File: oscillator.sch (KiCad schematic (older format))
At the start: 32 parts, among them Q1 PMOS, Q10 PMOS, Q11 MOS_Resistor, Q12 PMOS, Q13 PMOS, Q14 PMOS, Q15 MOS_Resistor, Q16 PMOS, Q17 PMOS, Q18 MOS_Resistor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

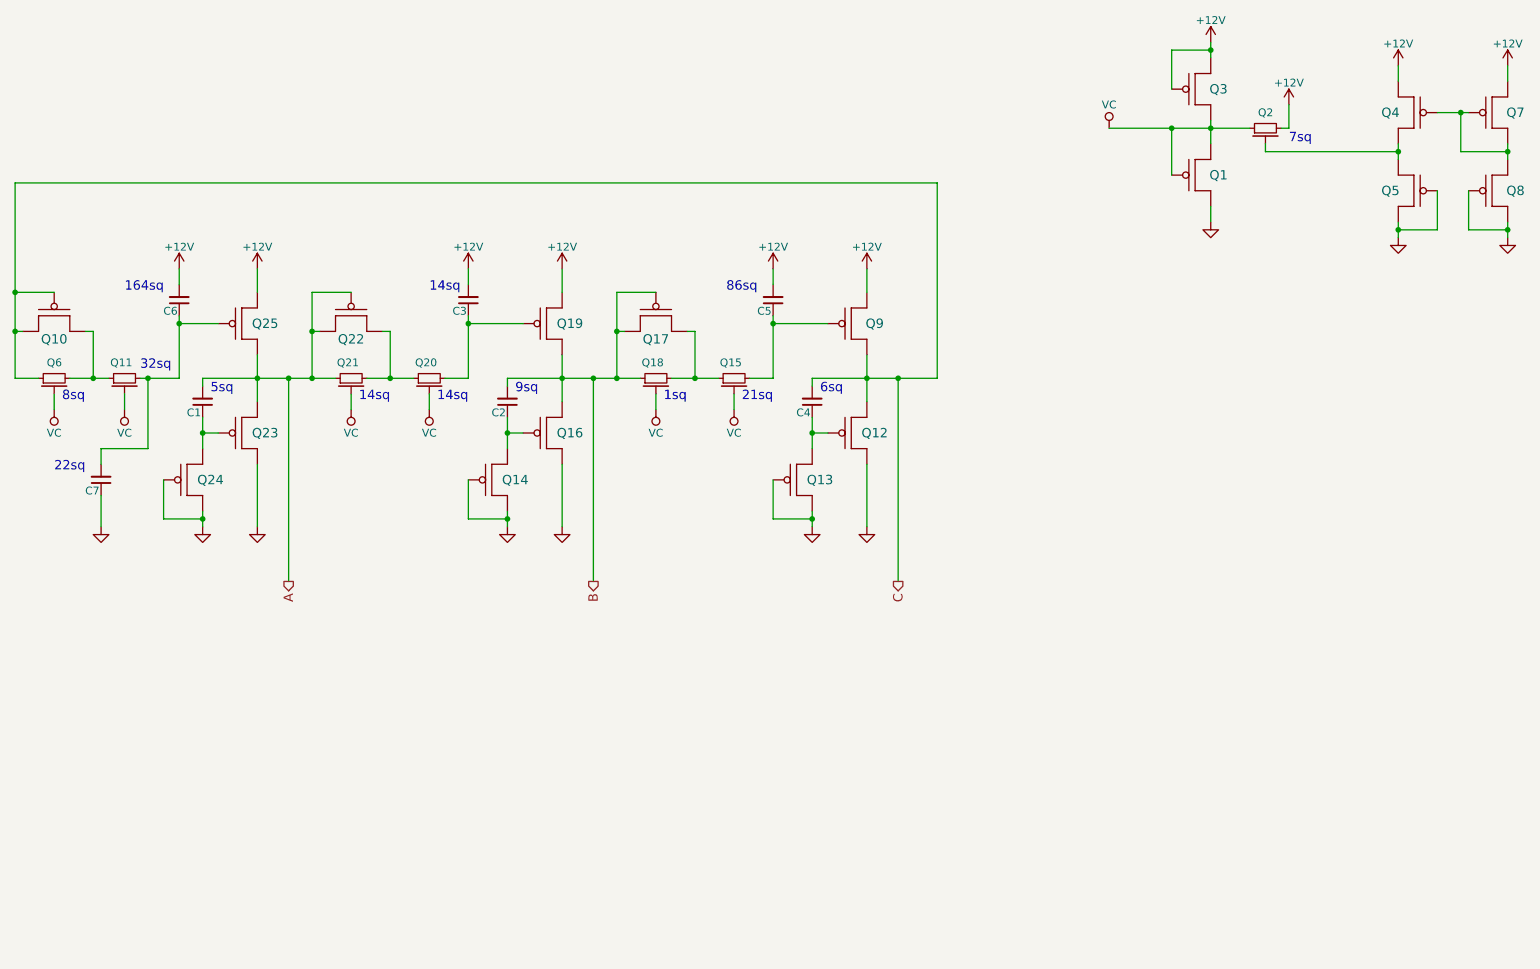
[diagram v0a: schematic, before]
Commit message: Adds clock phase generator schematics and PDFs, adds generic gates to mos.lib
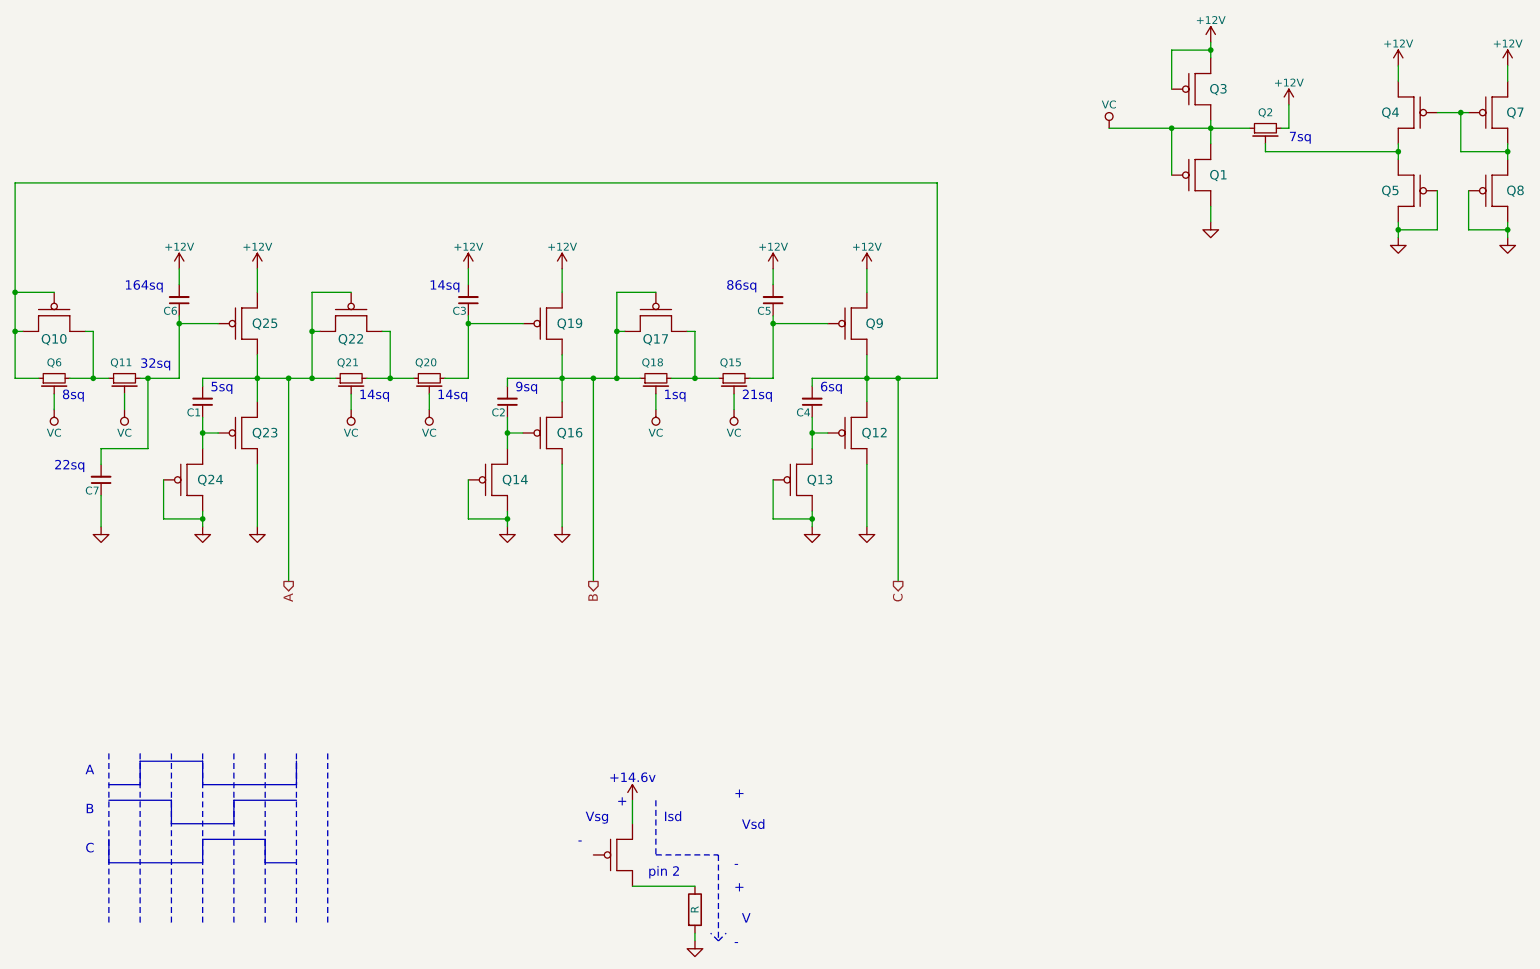
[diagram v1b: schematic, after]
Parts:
- added Q?: PMOS, symbol PMOS
- added R?: R, symbol R
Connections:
- net +12V: now also Q?.D
- net GND: now also R?.2
- new net: Q?.S, R?.1
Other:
- note added: "+"
- note added: "+14.6v"
- note added: "-"
- note added: "A"
- note added: "B"
- note added: "C"
- note added: "Isd"
- note added: "V"
- note added: "Vsd"
- note added: "Vsg"
- note added: "pin 2"
